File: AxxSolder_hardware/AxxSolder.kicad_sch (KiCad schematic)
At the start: 143 parts, among them IC1 TLV76733DRVR, IC2 OPA2387DSGT, IC3 LMR54406DBVR, IC4 STM32G431CBT6, IC5 TPD4E1U06DBVR, IC6 STUSB4500QTR, IC7 MAX16171ATA_VY+T, IC8 LTC4440AHMS8E, IC9 INA180A4IDBVT, J1 USB4110-GF-A, J2 691243110009, J3 TSW-102-07-T-S, J4 61300611821, J5 TSW-102-07-T-S, J6 TSW-102-07-T-S, Q1 STL9P3LLH6, Q2 STL10N3LLH5, Q3 2N7002NXAKR, U2 PEC11J-9215F-S0015, U3 BSC014N04LS

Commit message: Final changes after sending AxxSolder 3.0 for manufacturing
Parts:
- R44: Manufacturer_Name (none) -> Panasonic; Manufacturer_Part_Number (none) -> ERJ-6GEYJ105V; Mouser Part Number (none) -> 667-ERJ-6GEYJ105V
- R45: value 500m -> 560m; Manufacturer_Name (none) -> Panasonic; Manufacturer_Part_Number (none) -> ERJ-U6QJR56V; Mouser Part Number (none) -> 667-ERJ-U6QJR56V
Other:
- note added: "2024-02-18"
- note added: "SCREW TERMINAL AND EARTH LEAK SENSE"
- note removed: "2024-01-18"
- note removed: "SCREW TERMINAL"
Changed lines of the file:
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@@
     (effects (font (size 1.27 1.27)) (justify left bottom))
   )
-  (text "SCREW TERMINAL" (at 159.385 66.04 0)
+  (text "SCREW TERMINAL AND EARTH LEAK SENSE" (at 159.385 66.04 0)
     (effects (font (size 1.27 1.27)) (justify left bottom))
   )
@@
     (effects (font (size 1.27 1.27)) (justify left bottom))
   )
-  (text "2024-01-18" (at 206.375 194.31 0)
+  (text "2024-02-18" (at 206.375 194.31 0)
     (effects (font (size 1.27 1.27) bold (color 0 0 0 1)) (justify left bottom))
   )
@@
       (effects (font (size 1.27 1.27)) (justify left))
     )
-    (property "Value" "500m" (at 172.085 95.885 0)
+    (property "Value" "560m" (at 172.085 95.885 0)
       (effects (font (size 1.27 1.27)) (justify left))
     )
@@
       (effects (font (size 1.27 1.27)) hide)
     )
-    (property "Manufacturer_Name" "" (at 173.355 93.98 0)
-      (effects (font (size 1.27 1.27)) hide)
-    )
-    (property "Manufacturer_Part_Number" "" (at 173.355 93.98 0)
-      (effects (font (size 1.27 1.27)) hide)
-    )
-    (property "Mouser Part Number" "" (at 173.355 93.98 0)
+    (property "Manufacturer_Name" "Panasonic" (at 173.355 93.98 0)
+      (effects (font (size 1.27 1.27)) hide)
+    )
+    (property "Manufacturer_Part_Number" "ERJ-U6QJR56V" (at 173.355 93.98 0)
+      (effects (font (size 1.27 1.27)) hide)
+    )
+    (property "Mouser Part Number" "667-ERJ-U6QJR56V" (at 173.355 93.98 0)
       (effects (font (size 1.27 1.27)) hide)
     )
@@
       (effects (font (size 1.27 1.27)) hide)
     )
-    (property "Manufacturer_Name" "" (at 173.355 86.36 0)
-      (effects (font (size 1.27 1.27)) hide)
-    )
-    (property "Manufacturer_Part_Number" "" (at 173.355 86.36 0)
-      (effects (font (size 1.27 1.27)) hide)
-    )
-    (property "Mouser Part Number" "" (at 173.355 86.36 0)
-      (effects (font (size 1.27 1.27)) hide)
-    )
+    (property "Manufacturer_Name" "Panasonic" (at 173.355 86.36 0)
+      (effects (font (size 1.27 1.27)) hide)
+    )
+    (property "Manufacturer_Part_Number" "ERJ-6GEYJ105V" (at 173.355 86.36 0)
+      (effects (font (size 1.27 1.27)) hide)
+    )
+    (property "Mouser Part Number" "667-ERJ-6GEYJ105V" (at 173.355 86.36 0)
+      (effects (font (size 1.27 1.27)) hide)
+    )

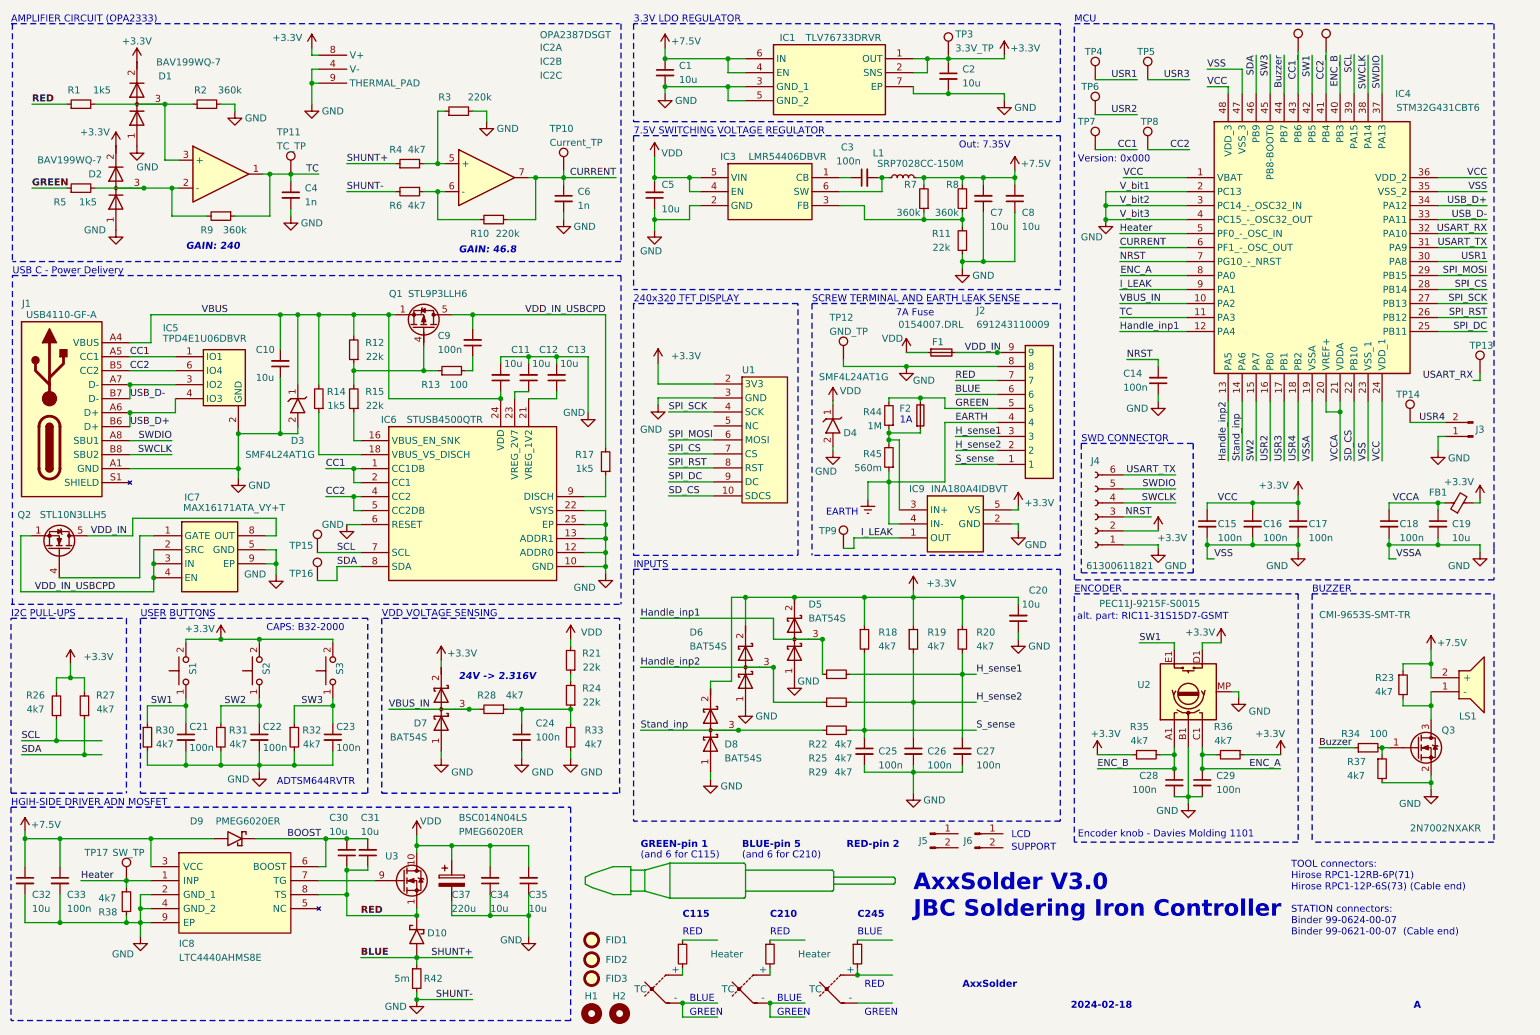
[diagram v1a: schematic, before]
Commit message: Update to new fuse and add alternative buzzer
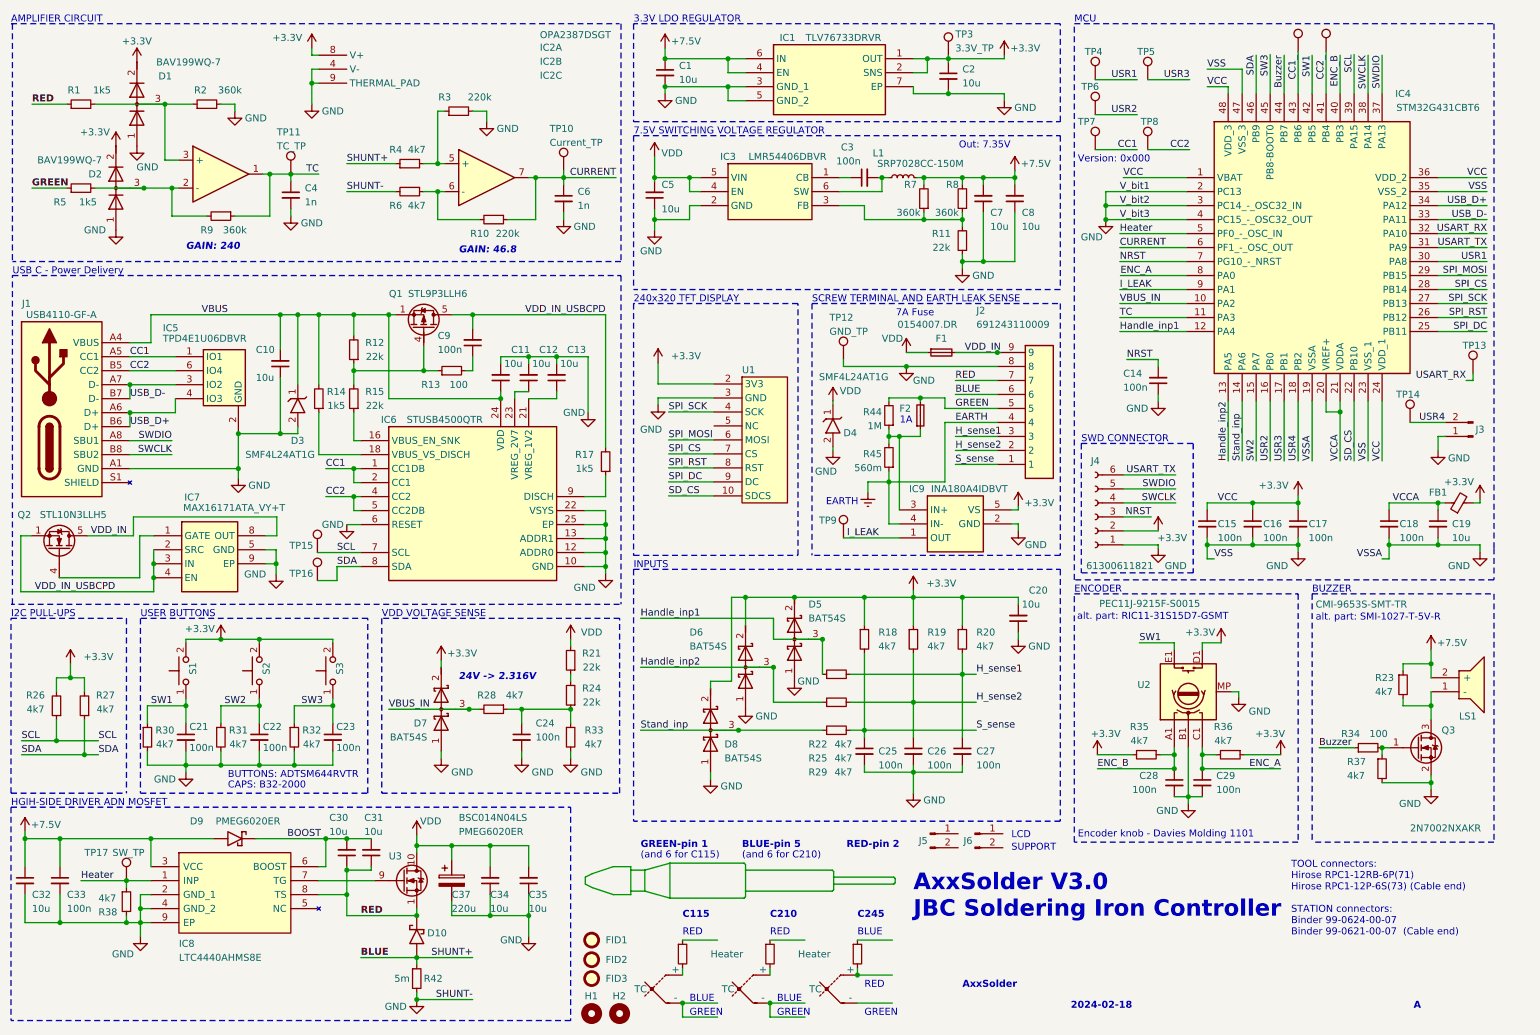
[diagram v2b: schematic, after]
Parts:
- removed F1: 0154007.DRL, footprints:0154100DR, symbol 0154007_DRL:0154007.DRL
- added F1: 0154007.DR, footprints:0154100DR, symbol 0154007_DR:0154007.DRL
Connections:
- net VDD: now also F1.1
- net VDD_IN: now also F1.2
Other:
- note added: "AMPLIFIER CIRCUIT"
- note added: "BUTTONS: ADTSM644RVTR"
- note added: "VDD VOLTAGE SENSE"
- note added: "alt. part: SMI-1027-T-5V-R"
- note removed: "ADTSM644RVTR"
- note removed: "AMPLIFIER CIRCUIT (OPA2333)"
- note removed: "VDD VOLTAGE SENSING"
- moved on the sheet: C31, TP13, TP9

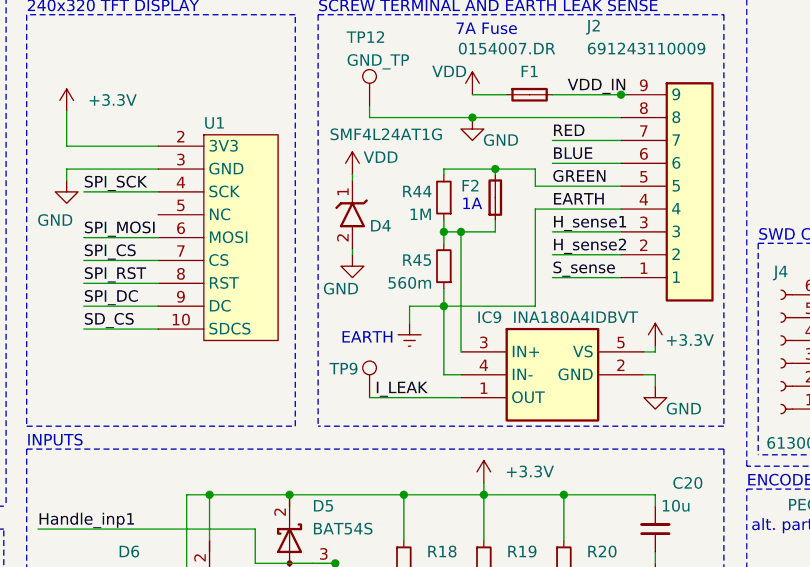
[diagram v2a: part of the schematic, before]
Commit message: update current sense resistor to 100m ohm from 560m ohm
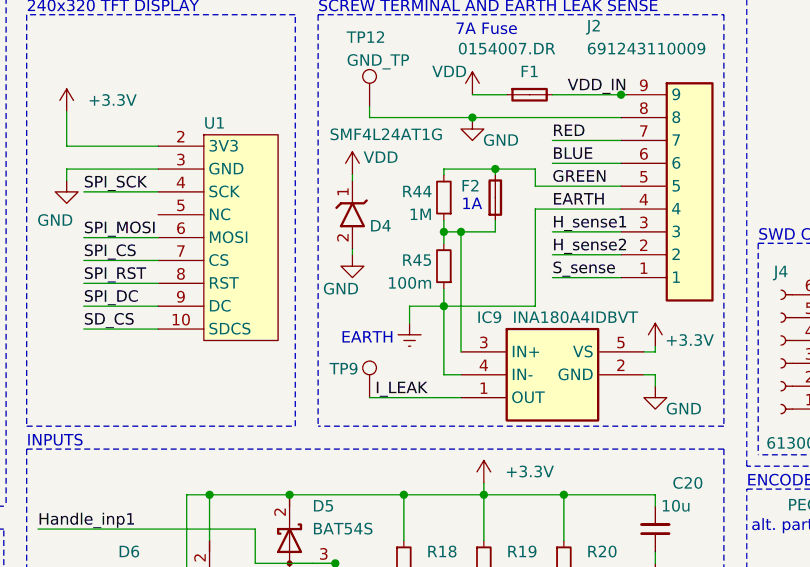
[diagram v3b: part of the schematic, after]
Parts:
- R45: value 560m -> 100m; Manufacturer_Part_Number ERJ-U6QJR56V -> ERJ-6DSFR10V; Mouser Part Number 667-ERJ-U6QJR56V -> 667-ERJ-6DSFR10V
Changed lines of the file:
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@@
       (effects (font (size 1.27 1.27)) (justify left))
     )
-    (property "Value" "560m" (at 172.085 95.885 0)
+    (property "Value" "100m" (at 172.085 95.885 0)
       (effects (font (size 1.27 1.27)) (justify left))
     )
@@
       (effects (font (size 1.27 1.27)) hide)
     )
-    (property "Manufacturer_Part_Number" "ERJ-U6QJR56V" (at 173.355 93.98 0)
+    (property "Manufacturer_Part_Number" "ERJ-6DSFR10V" (at 173.355 93.98 0)
       (effects (font (size 1.27 1.27)) hide)
     )
-    (property "Mouser Part Number" "667-ERJ-U6QJR56V" (at 173.355 93.98 0)
+    (property "Mouser Part Number" "667-ERJ-6DSFR10V" (at 173.355 93.98 0)
       (effects (font (size 1.27 1.27)) hide)
     )

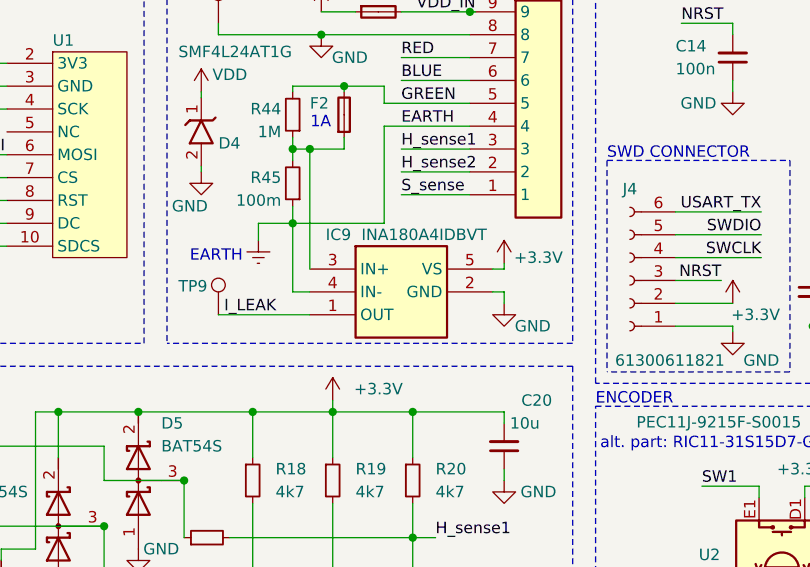
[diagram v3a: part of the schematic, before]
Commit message: Change IC9 from INA180 to INA281
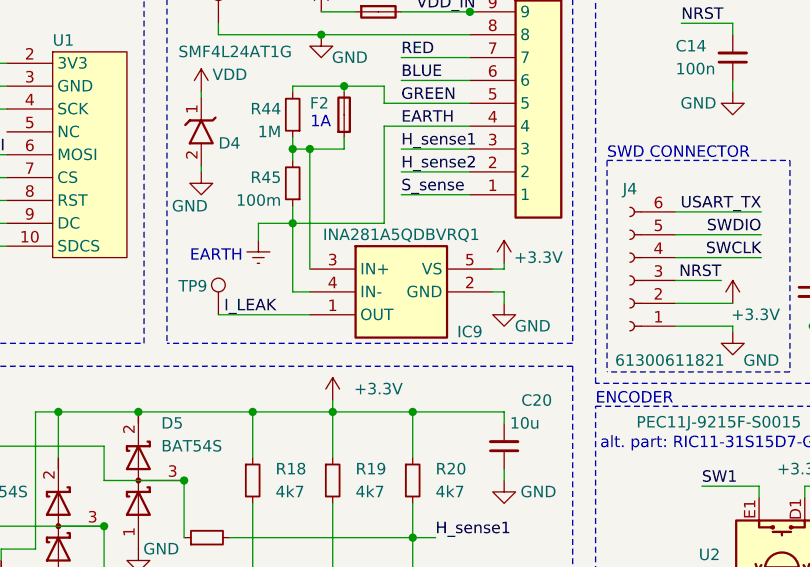
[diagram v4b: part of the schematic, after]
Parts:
- removed IC9: INA180A4IDBVT, footprints:SOT95P280X145-5N, symbol INA180A4IDBVT:INA180A4IDBVT
- added IC9: INA281A5QDBVRQ1, footprints:SOT95P280X145-5N, symbol INA281A5QDBVRQ1:INA281A5QDBVRQ1
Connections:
- net +3.3V: now also IC9.5 (VS)
- net Earth: now also IC9.4 (IN-)
- net GND: now also IC9.2 (GND)
- net I_LEAK: now also IC9.1 (OUT)
- net at F2.1, R44.1, R45.2: now also IC9.3 (IN+)
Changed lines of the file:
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@@
+    )
+  )
+  (symbol (lib_id "INA281A5QDBVRQ1:INA281A5QDBVRQ1") (at 175.26 103.505 0) (unit 1)
+    (in_bom yes) (on_board yes) (dnp no)
+    (property "Reference" "IC9" (at 193.04 110.49 0)
+      (effects (font (size 1.27 1.27)))
+    )
+    (property "Value" "INA281A5QDBVRQ1" (at 185.42 99.695 0)
+      (effects (font (size 1.27 1.27)))
+    )
+    (property "Footprint" "footprints:SOT95P280X145-5N" (at 196.85 198.425 0)
+      (effects (font (size 1.27 1.27)) (justify left top) hide)
+    )
+    (property "Datasheet" "https://www.ti.com/lit/ds/symlink/ina281-q1.pdf" (at 196.85 298.425 0)
+      (effects (font (size 1.27 1.27)) (justify left top) hide)
+    )
+    (property "Height" "1.45" (at 196.85 498.425 0)
+      (effects (font (size 1.27 1.27)) (justify left top) hide)
+    )
+    (property "Mouser Part Number" "595-INA281A5QDBVRQ1" (at 196.85 598.425 0)
+      (effects (font (size 1.27 1.27)) (justify left top) hide)
+    )
+    (property "Mouser Price/Stock" "https://www.mouser.co.uk/ProductDetail/Texas-Instruments/INA281A5QDBVRQ1?qs=hd1VzrDQEGgwv71iGabWgQ%3D%3D" (at 196.85 698.425 0)
+      (effects (font (size 1.27 1.27)) (justify left top) hide)
+    )
+    (property "Manufacturer_Name" "Texas Instruments" (at 196.85 798.425 0)
+      (effects (font (size 1.27 1.27)) (justify left top) hide)
+    )
+    (property "Manufacturer_Part_Number" "INA281A5QDBVRQ1" (at 196.85 898.425 0)
+      (effects (font (size 1.27 1.27)) (justify left top) hide)
+    )
+    (pin "1")
+    (pin "3")
+    (pin "2")
+    (pin "5")
+    (pin "4")
+    (instances
+      (project "AxxSolder"
+        (path "/d71363c3-4d90-469c-a600-831e2a7cdaef"
+          (reference "IC9") (unit 1)
+        )
+      )
     )
   )
@@
         )
       )
-    )
-  )
-  (symbol (lib_id "INA180A4IDBVT:INA180A4IDBVT") (at 175.26 103.505 0) (unit 1)
-    (in_bom yes) (on_board yes) (dnp no)
-    (property "Reference" "IC9" (at 178.435 99.695 0)
-      (effects (font (size 1.27 1.27)))
-    )
-    (property "Value" "INA180A4IDBVT" (at 187.96 99.695 0)
-      (effects (font (size 1.27 1.27)))
-    )
-    (property "Footprint" "footprints:SOT95P280X145-5N" (at 196.85 198.425 0)
-      (effects (font (size 1.27 1.27)) (justify left top) hide)
-    )
-    (property "Datasheet" "http://www.ti.com/lit/gpn/ina180" (at 196.85 298.425 0)
-      (effects (font (size 1.27 1.27)) (justify left top) hide)
-    )
-    (property "Height" "1.45" (at 196.85 498.425 0)
-      (effects (font (size 1.27 1.27)) (justify left top) hide)
-    )
-    (property "Mouser Part Number" "595-INA180A4IDBVT" (at 196.85 598.425 0)
-      (effects (font (size 1.27 1.27)) (justify left top) hide)
-    )
-    (property "Mouser Price/Stock" "https://www.mouser.co.uk/ProductDetail/Texas-Instruments/INA180A4IDBVT?qs=5aG0NVq1C4zRWLlwoLPFOA%3D%3D" (at 196.85 698.425 0)
-      (effects (font (size 1.27 1.27)) (justify left top) hide)
-    )
-    (property "Manufacturer_Name" "Texas Instruments" (at 196.85 798.425 0)
-      (effects (font (size 1.27 1.27)) (justify left top) hide)
-    )
-    (property "Manufacturer_Part_Number" "INA180A4IDBVT" (at 196.85 898.425 0)
-      (effects (font (size 1.27 1.27)) (justify left top) hide)
-    )
-    (pin "2")
-    (pin "4")
-    (pin "1")
-    (pin "3")
-    (pin "5")
-    (instances
-      (project "AxxSolder"
-        (path "/d71363c3-4d90-469c-a600-831e2a7cdaef"
-          (reference "IC9") (unit 1)
-        )
-      )

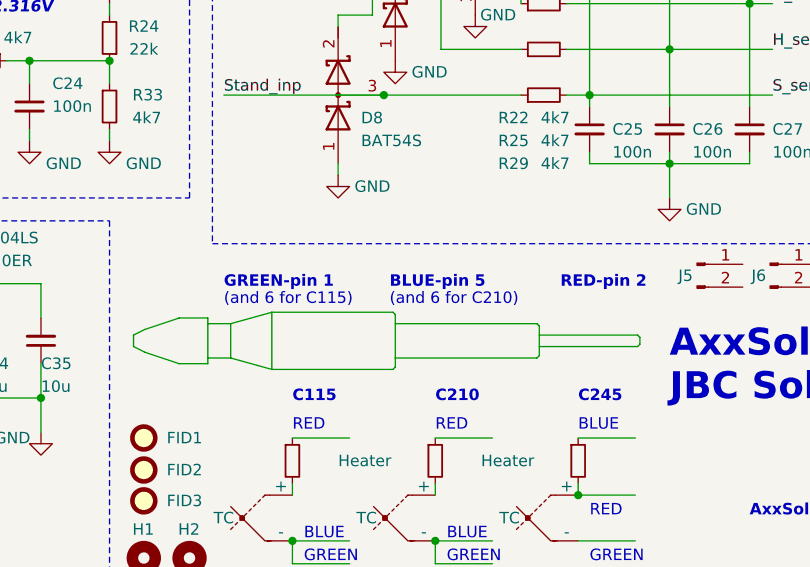
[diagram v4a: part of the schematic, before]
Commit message: Update NT115 handle connector pin jumer position
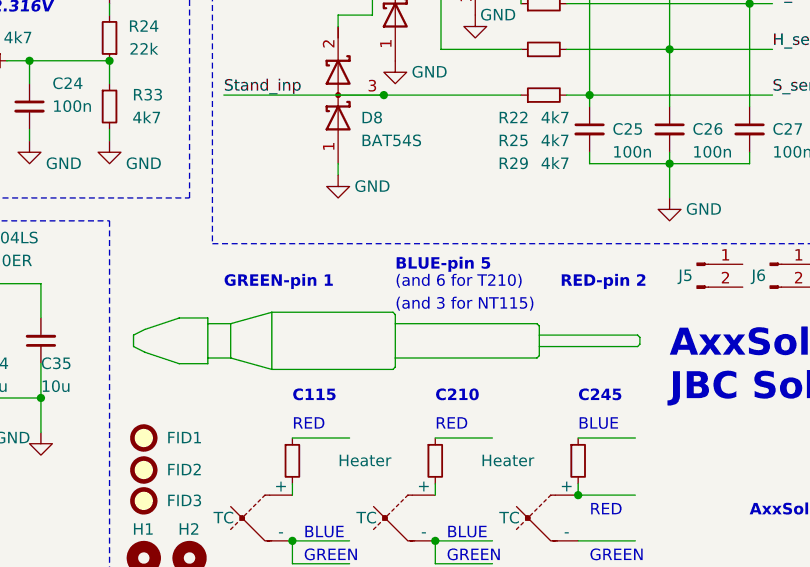
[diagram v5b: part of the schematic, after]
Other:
- note added: "(and 3 for NT115)"
- note added: "(and 6 for T210)"
- note removed: "(and 6 for C115)"
- note removed: "(and 6 for C210)"
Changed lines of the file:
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@@
+    (effects (font (size 1.27 1.27)) (justify left bottom))
+  )
+  (text "(and 3 for NT115)" (at 147.32 167.64 0)
     (effects (font (size 1.27 1.27)) (justify left bottom))
   )
@@
     (effects (font (size 1.27 1.27)) (justify left bottom))
   )
-  (text "(and 6 for C210)" (at 146.685 167.005 0)
+  (text "(and 6 for T210)" (at 147.32 165.1 0)
     (effects (font (size 1.27 1.27)) (justify left bottom))
   )
@@
     (effects (font (size 1.27 1.27)) (justify left bottom))
   )
-  (text "BLUE-pin 5" (at 146.685 165.1 0)
+  (text "BLUE-pin 5" (at 147.32 163.195 0)
     (effects (font (size 1.27 1.27) (thickness 0.254) bold) (justify left bottom))
   )
@@
     (effects (font (size 1.27 1.27)) (justify left bottom))
   )
-  (text "(and 6 for C115)" (at 128.27 167.005 0)
-    (effects (font (size 1.27 1.27) (color 0 132 0 1)) (justify left bottom))
-  )
   (text "alt. part: RIC11-31S15D7-GSMT\n" (at 207.518 123.698 0)

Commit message: Update and add data for backside manufacturing and assembly
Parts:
- FID1, FID2, FID3, H1, H2, J2, J3, J4, J5, J6, R39, R40, R41, TC1, TC2, TC3, TP1, TP10, TP11, TP12, TP13, TP14, TP15, TP16, TP17, TP2, TP3, TP4, TP5, TP6, TP7, TP8, TP9, U1: Manufacturing comment (none) -> Do Not Place
